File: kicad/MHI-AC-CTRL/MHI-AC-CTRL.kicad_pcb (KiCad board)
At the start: 2 copper layers, 41.9 x 27.2 mm, 9 parts, among them J1 Conn_01x05, J3 Conn_01x03, U1 TSR_1-2450, U2 WeMos_D1_mini, U3 LEVEL-SHIFTER-4CH

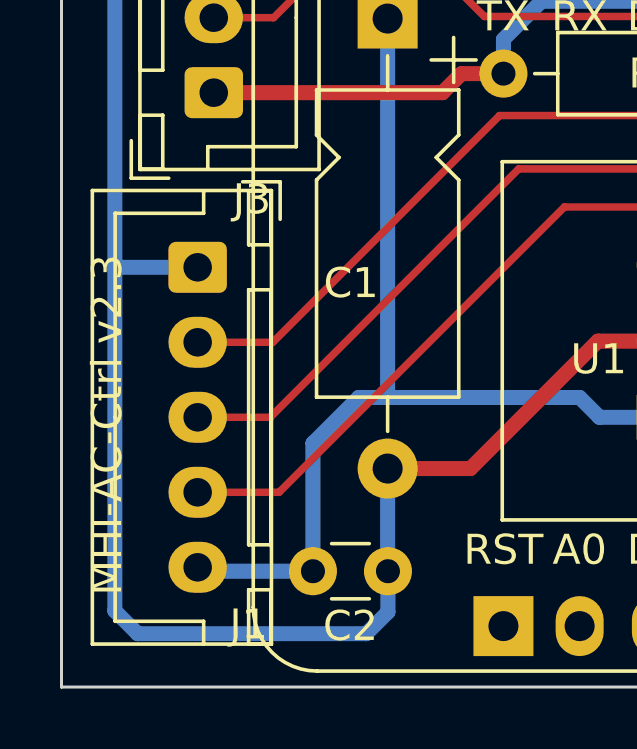
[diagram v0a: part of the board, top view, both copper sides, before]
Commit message: kicad: Move connector to the bottom of the PCB
This changes the appearance of the connector only! The pin-out remains
identical, the gerbers, identical. Only the location of the connector
moved, which causes the silkscreen to change and the 3D render.

Signed-off-by: Olliver Schinagl <oliver@schinagl.nl>
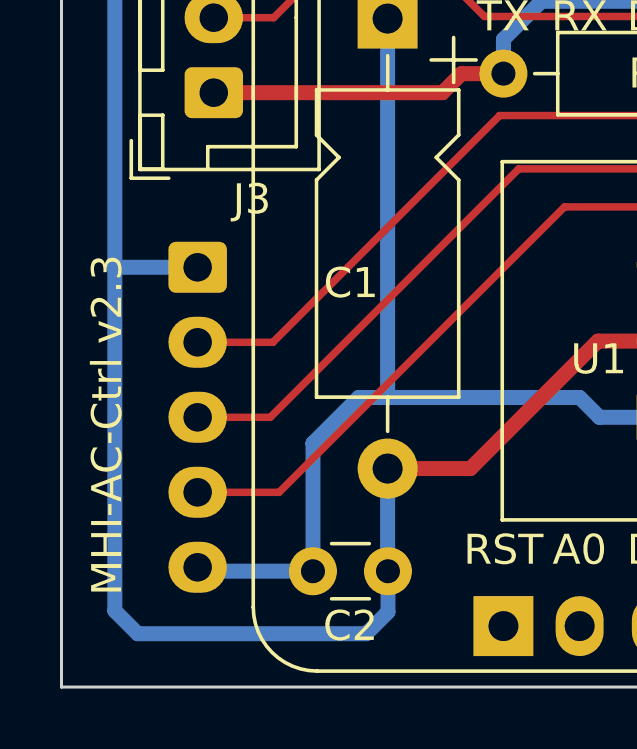
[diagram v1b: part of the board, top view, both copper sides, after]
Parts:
- J1: moved to B.Cu
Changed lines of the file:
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@@
-    )
-  )
-  (footprint "Connector_JST:JST_XH_B5B-XH-A_1x05_P2.50mm_Vertical" (layer "F.Cu")
-    (at 83.7862 50.2704 -90)
-    (descr "JST XH series connector, B5B-XH-A (http://www.jst-mfg.com/product/pdf/eng/eXH.pdf), generated with kicad-footprint-generator")
-    (tags "connector JST XH vertical")
-    (property "Sheetfile" "File: MHI-AC-CTRL.kicad_sch")
-    (property "Sheetname" "")
-    (attr through_hole)
-    (fp_text reference "J1" (at 11.9088 -1.7 180) (layer "F.SilkS")
-      (effects (font (size 1 1) (thickness 0.15)))
-    )
-    (fp_text value "Conn_01x05" (at 5 4.6 90) (layer "F.Fab")
-      (effects (font (size 1 1) (thickness 0.15)))
-    )
-    (fp_text user "${REFERENCE}" (at 5 2.7 90) (layer "F.Fab")
-      (effects (font (size 1 1) (thickness 0.15)))
-    )
-    (fp_line (start -2.55 -1.7) (end -0.75 -1.7) (layer "F.SilkS") (width 0.12))
-    (fp_line (start 12.55 -2.45) (end 10.75 -2.45) (layer "F.SilkS") (width 0.12))
-    (fp_line (start -2.56 -2.46) (end -2.56 3.51) (layer "F.SilkS") (width 0.12))
-    (fp_line (start -2.85 -2.75) (end -2.85 -1.5) (layer "F.SilkS") (width 0.12))
-    (fp_line (start -1.8 2.75) (end 5 2.75) (layer "F.SilkS") (width 0.12))
-    (fp_line (start 10.75 -1.7) (end 12.55 -1.7) (layer "F.SilkS") (width 0.12))
-    (fp_line (start 0.75 -1.7) (end 9.25 -1.7) (layer "F.SilkS") (width 0.12))
-    (fp_line (start 11.8 -0.2) (end 11.8 2.75) (layer "F.SilkS") (width 0.12))
-    (fp_line (start -1.6 -2.75) (end -2.85 -2.75) (layer "F.SilkS") (width 0.12))
-    (fp_line (start -0.75 -2.45) (end -2.55 -2.45) (layer "F.SilkS") (width 0.12))
-    (fp_line (start -2.55 -0.2) (end -1.8 -0.2) (layer "F.SilkS") (width 0.12))
-    (fp_line (start -2.56 3.51) (end 12.56 3.51) (layer "F.SilkS") (width 0.12))
-    (fp_line (start 12.56 -2.46) (end -2.56 -2.46) (layer "F.SilkS") (width 0.12))
-    (fp_line (start -0.75 -1.7) (end -0.75 -2.45) (layer "F.SilkS") (width 0.12))
-    (fp_line (start 10.75 -2.45) (end 10.75 -1.7) (layer "F.SilkS") (width 0.12))
-    (fp_line (start 11.8 2.75) (end 5 2.75) (layer "F.SilkS") (width 0.12))
-    (fp_line (start 9.25 -2.45) (end 0.75 -2.45) (layer "F.SilkS") (width 0.12))
-    (fp_line (start 12.55 -0.2) (end 11.8 -0.2) (layer "F.SilkS") (width 0.12))
-    (fp_line (start -2.55 -2.45) (end -2.55 -1.7) (layer "F.SilkS") (width 0.12))
-    (fp_line (start 0.75 -2.45) (end 0.75 -1.7) (layer "F.SilkS") (width 0.12))
-    (fp_line (start -1.8 -0.2) (end -1.8 2.75) (layer "F.SilkS") (width 0.12))
-    (fp_line (start 12.56 3.51) (end 12.56 -2.46) (layer "F.SilkS") (width 0.12))
-    (fp_line (start 12.55 -1.7) (end 12.55 -2.45) (layer "F.SilkS") (width 0.12))
-    (fp_line (start 9.25 -1.7) (end 9.25 -2.45) (layer "F.SilkS") (width 0.12))
-    (fp_line (start -2.95 -2.85) (end -2.95 3.9) (layer "F.CrtYd") (width 0.05))
-    (fp_line (start 12.95 -2.85) (end -2.95 -2.85) (layer "F.CrtYd") (width 0.05))
-    (fp_line (start 12.95 3.9) (end 12.95 -2.85) (layer "F.CrtYd") (width 0.05))
-    (fp_line (start -2.95 3.9) (end 12.95 3.9) (layer "F.CrtYd") (width 0.05))
-    (fp_line (start 12.45 -2.35) (end -2.45 -2.35) (layer "F.Fab") (width 0.1))
-    (fp_line (start -2.45 -2.35) (end -2.45 3.4) (layer "F.Fab") (width 0.1))
-    (fp_line (start -0.625 -2.35) (end 0 -1.35) (layer "F.Fab") (width 0.1))
-    (fp_line (start 0 -1.35) (end 0.625 -2.35) (layer "F.Fab") (width 0.1))
-    (fp_line (start -2.45 3.4) (end 12.45 3.4) (layer "F.Fab") (width 0.1))
-    (fp_line (start 12.45 3.4) (end 12.45 -2.35) (layer "F.Fab") (width 0.1))
-    (pad "1" thru_hole roundrect (at 0 0 270) (size 1.7 1.95) (drill 0.95) (layers *.Cu *.Mask) (roundrect_rratio 0.1470588235)
-      (net 2 "GND") (pinfunction "Pin_1") (pintype "passive"))
-    (pad "2" thru_hole oval (at 2.5 0 270) (size 1.7 1.95) (drill 0.95) (layers *.Cu *.Mask)
-      (net 4 "MISO_5V") (pinfunction "Pin_2") (pintype "passive"))
-    (pad "3" thru_hole oval (at 5 0 270) (size 1.7 1.95) (drill 0.95) (layers *.Cu *.Mask)
-      (net 5 "MOSI_5V") (pinfunction "Pin_3") (pintype "passive"))
-    (pad "4" thru_hole oval (at 7.5 0 270) (size 1.7 1.95) (drill 0.95) (layers *.Cu *.Mask)
-      (net 6 "CLK_5V") (pinfunction "Pin_4") (pintype "passive"))
-    (pad "5" thru_hole oval (at 10 0 270) (size 1.7 1.95) (drill 0.95) (layers *.Cu *.Mask)
-      (net 1 "+12V") (pinfunction "Pin_5") (pintype "passive"))
-    (model "${KICAD6_3DMODEL_DIR}/Connector_JST.3dshapes/JST_XH_B5B-XH-A_1x05_P2.50mm_Vertical.wrl"
-      (offset (xyz 0 0 0))
-      (scale (xyz 1 1 1))
-      (rotate (xyz 0 0 0))
     )
   )
@@
       (offset (xyz 0 0 0))
       (scale (xyz 1 1 1))
+      (rotate (xyz 0 0 0))
+    )
+  )
+  (footprint "Connector_JST:JST_XH_B5B-XH-A_1x05_P2.50mm_Vertical" (layer "B.Cu")
+    (at 83.7862 50.2704 -90)
+    (descr "JST XH series connector, B5B-XH-A (http://www.jst-mfg.com/product/pdf/eng/eXH.pdf), generated with kicad-footprint-generator")
+    (tags "connector JST XH vertical")
+    (property "Sheetfile" "File: MHI-AC-CTRL.kicad_sch")
+    (property "Sheetname" "")
+    (attr through_hole)
+    (fp_text reference "J1" (at 11.9088 1.7) (layer "B.SilkS")
+      (effects (font (size 1 1) (thickness 0.15)) (justify mirror))
+    )
+    (fp_text value "Conn_01x05" (at 5 -4.6 90) (layer "B.Fab")
+      (effects (font (size 1 1) (thickness 0.15)) (justify mirror))
+    )
+    (fp_text user "${REFERENCE}" (at 5 -2.7 90) (layer "B.Fab")
+      (effects (font (size 1 1) (thickness 0.15)) (justify mirror))
+    )
+    (fp_line (start -2.55 1.7) (end -0.75 1.7) (layer "B.SilkS") (width 0.12))
+    (fp_line (start 12.55 2.45) (end 10.75 2.45) (layer "B.SilkS") (width 0.12))
+    (fp_line (start -2.56 2.46) (end -2.56 -3.51) (layer "B.SilkS") (width 0.12))
+    (fp_line (start -2.85 2.75) (end -2.85 1.5) (layer "B.SilkS") (width 0.12))
+    (fp_line (start -1.8 -2.75) (end 5 -2.75) (layer "B.SilkS") (width 0.12))
+    (fp_line (start 10.75 1.7) (end 12.55 1.7) (layer "B.SilkS") (width 0.12))
+    (fp_line (start 0.75 1.7) (end 9.25 1.7) (layer "B.SilkS") (width 0.12))
+    (fp_line (start 11.8 0.2) (end 11.8 -2.75) (layer "B.SilkS") (width 0.12))
+    (fp_line (start -1.6 2.75) (end -2.85 2.75) (layer "B.SilkS") (width 0.12))
+    (fp_line (start -0.75 2.45) (end -2.55 2.45) (layer "B.SilkS") (width 0.12))
+    (fp_line (start -2.55 0.2) (end -1.8 0.2) (layer "B.SilkS") (width 0.12))
+    (fp_line (start -2.56 -3.51) (end 12.56 -3.51) (layer "B.SilkS") (width 0.12))
+    (fp_line (start 12.56 2.46) (end -2.56 2.46) (layer "B.SilkS") (width 0.12))
+    (fp_line (start -0.75 1.7) (end -0.75 2.45) (layer "B.SilkS") (width 0.12))
+    (fp_line (start 10.75 2.45) (end 10.75 1.7) (layer "B.SilkS") (width 0.12))
+    (fp_line (start 11.8 -2.75) (end 5 -2.75) (layer "B.SilkS") (width 0.12))
+    (fp_line (start 9.25 2.45) (end 0.75 2.45) (layer "B.SilkS") (width 0.12))
+    (fp_line (start 12.55 0.2) (end 11.8 0.2) (layer "B.SilkS") (width 0.12))
+    (fp_line (start -2.55 2.45) (end -2.55 1.7) (layer "B.SilkS") (width 0.12))
+    (fp_line (start 0.75 2.45) (end 0.75 1.7) (layer "B.SilkS") (width 0.12))
+    (fp_line (start -1.8 0.2) (end -1.8 -2.75) (layer "B.SilkS") (width 0.12))
+    (fp_line (start 12.56 -3.51) (end 12.56 2.46) (layer "B.SilkS") (width 0.12))
+    (fp_line (start 12.55 1.7) (end 12.55 2.45) (layer "B.SilkS") (width 0.12))
+    (fp_line (start 9.25 1.7) (end 9.25 2.45) (layer "B.SilkS") (width 0.12))
+    (fp_line (start -2.95 2.85) (end -2.95 -3.9) (layer "B.CrtYd") (width 0.05))
+    (fp_line (start 12.95 2.85) (end -2.95 2.85) (layer "B.CrtYd") (width 0.05))
+    (fp_line (start 12.95 -3.9) (end 12.95 2.85) (layer "B.CrtYd") (width 0.05))
+    (fp_line (start -2.95 -3.9) (end 12.95 -3.9) (layer "B.CrtYd") (width 0.05))
+    (fp_line (start 12.45 2.35) (end -2.45 2.35) (layer "B.Fab") (width 0.1))
+    (fp_line (start -2.45 2.35) (end -2.45 -3.4) (layer "B.Fab") (width 0.1))
+    (fp_line (start -0.625 2.35) (end 0 1.35) (layer "B.Fab") (width 0.1))
+    (fp_line (start 0 1.35) (end 0.625 2.35) (layer "B.Fab") (width 0.1))
+    (fp_line (start -2.45 -3.4) (end 12.45 -3.4) (layer "B.Fab") (width 0.1))
+    (fp_line (start 12.45 -3.4) (end 12.45 2.35) (layer "B.Fab") (width 0.1))
+    (pad "1" thru_hole roundrect (at 0 0 270) (size 1.7 1.95) (drill 0.95) (layers *.Cu *.Mask) (roundrect_rratio 0.1470588235)
+      (net 2 "GND") (pinfunction "Pin_1") (pintype "passive"))
+    (pad "2" thru_hole oval (at 2.5 0 270) (size 1.7 1.95) (drill 0.95) (layers *.Cu *.Mask)
+      (net 4 "MISO_5V") (pinfunction "Pin_2") (pintype "passive"))
+    (pad "3" thru_hole oval (at 5 0 270) (size 1.7 1.95) (drill 0.95) (layers *.Cu *.Mask)
+      (net 5 "MOSI_5V") (pinfunction "Pin_3") (pintype "passive"))
+    (pad "4" thru_hole oval (at 7.5 0 270) (size 1.7 1.95) (drill 0.95) (layers *.Cu *.Mask)
+      (net 6 "CLK_5V") (pinfunction "Pin_4") (pintype "passive"))
+    (pad "5" thru_hole oval (at 10 0 270) (size 1.7 1.95) (drill 0.95) (layers *.Cu *.Mask)
+      (net 1 "+12V") (pinfunction "Pin_5") (pintype "passive"))
+    (model "${KICAD6_3DMODEL_DIR}/Connector_JST.3dshapes/JST_XH_B5B-XH-A_1x05_P2.50mm_Vertical.wrl"
+      (offset (xyz 0 0 0))
+      (scale (xyz 1 1 1))
